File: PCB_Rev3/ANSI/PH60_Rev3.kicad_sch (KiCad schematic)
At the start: 46 parts, among them J1 USB_C_Receptacle_USB2.0_16P, J2 Conn_01x02, J3 Conn_01x02_Pin, J4 Conn_01x02_Pin, J6 Conn_01x02_Pin, SW1 SW_SPDT_321, U1 TLV62569DBV, U2 RP2040, U4 ETA6093, U6 W25Q16JVSS, Y1 Crystal_GND24

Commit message: Antenna update
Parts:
- added J8: Conn_01x02_Pin, Connector_PinHeader_2.00mm:PinHeader_1x02_P2.00mm_Vertical, symbol Connector:Conn_01x02_Pin
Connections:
- net RPI_TX: now reaches U2.40 (GPIO28_ADC2)
- net RPI_TX: now also J8.2 (Pin_2)
- net RPI_RX: now reaches U2.41 (GPIO29_ADC3)
- net RPI_RX: now also J8.1 (Pin_1)
- no-connect marks 12 -> 10
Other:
- moved on the sheet: J3, J4, J6

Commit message: vbus layout
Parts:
- added C27: 100uF, Capacitor_SMD:C_1206_3216Metric, symbol Device:C
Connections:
- net GND: now also C27.1
- net VBUS_SW: now also C27.2
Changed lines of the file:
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@@
 	)
 	(junction
+		(at 45.72 97.79)
+		(diameter 0)
+		(color 0 0 0 0)
+	)
+	(junction
 		(at 196.85 36.83)
 		(diameter 0)
@@
 	)
 	(symbol
+		(lib_id "power:GND")
+		(at 38.1 97.79 180)
+		(unit 1)
+		(exclude_from_sim no)
+		(in_bom yes)
+		(on_board yes)
+		(dnp no)
+		(fields_autoplaced yes)
+		(property "Reference" "#PWR041"
+			(at 38.1 91.44 0)
+			(effects
+				(font
+					(size 1.27 1.27)
+				)
+				(hide yes)
+			)
+		)
+		(property "Value" "GND"
+			(at 38.1 92.71 0)
+			(effects
+				(font
+					(size 1.27 1.27)
+				)
+			)
+		)
+		(property "Footprint" ""
+			(at 38.1 97.79 0)
+			(effects
+				(font
+					(size 1.27 1.27)
+				)
+				(hide yes)
+			)
+		)
+		(property "Datasheet" ""
+			(at 38.1 97.79 0)
+			(effects
+				(font
+					(size 1.27 1.27)
+				)
+				(hide yes)
+			)
+		)
+		(property "Description" "Power symbol creates a global label with name \"GND\" , ground"
+			(at 38.1 97.79 0)
+			(effects
+				(font
+					(size 1.27 1.27)
+				)
+				(hide yes)
+			)
+		)
+		(pin "1"
+		)
+		(instances
+			(project "PH60_Rev3"
+				(path "/dca0f898-8fdb-4522-a51d-f4f4238906e7"
+					(reference "#PWR041")
+					(unit 1)
+				)
+			)
+		)
+	)
+	(symbol
 		(lib_id "Device:C")
 		(at 113.03 43.18 0)
@@
 					(unit 1)
 				)
+			)
+		)
+	)
+	(symbol
+		(lib_id "Device:C")
+		(at 41.91 97.79 90)
+		(unit 1)
+		(exclude_from_sim no)
+		(in_bom no)
+		(on_board yes)
+		(dnp no)
+		(fields_autoplaced yes)
+		(property "Reference" "C27"
+			(at 41.91 90.17 90)
+			(effects
+				(font
+					(size 1.27 1.27)
+				)
+			)
+		)
+		(property "Value" "100uF"
+			(at 41.91 92.71 90)
+			(effects
+				(font
+					(size 1.27 1.27)
+				)
+			)
+		)
+		(property "Footprint" "Capacitor_SMD:C_1206_3216Metric"
+			(at 45.72 96.8248 0)
+			(effects
+				(font
+					(size 1.27 1.27)
+				)
+				(hide yes)
+			)
+		)
+		(property "Datasheet" "~"
+			(at 41.91 97.79 0)
+			(effects
+				(font
+					(size 1.27 1.27)
+				)
+				(hide yes)
+			)
+		)
+		(property "Description" "Unpolarized capacitor"
+			(at 41.91 97.79 0)
+			(effects
+				(font
+					(size 1.27 1.27)
+				)
+				(hide yes)
+			)
+		)
+		(pin "2"
+		)
+		(pin "1"
+		)
+		(instances
+			(project "PH60_Rev3"
+				(path "/dca0f898-8fdb-4522-a51d-f4f4238906e7"
+					(reference "C27")
+					(unit 1)
+				)

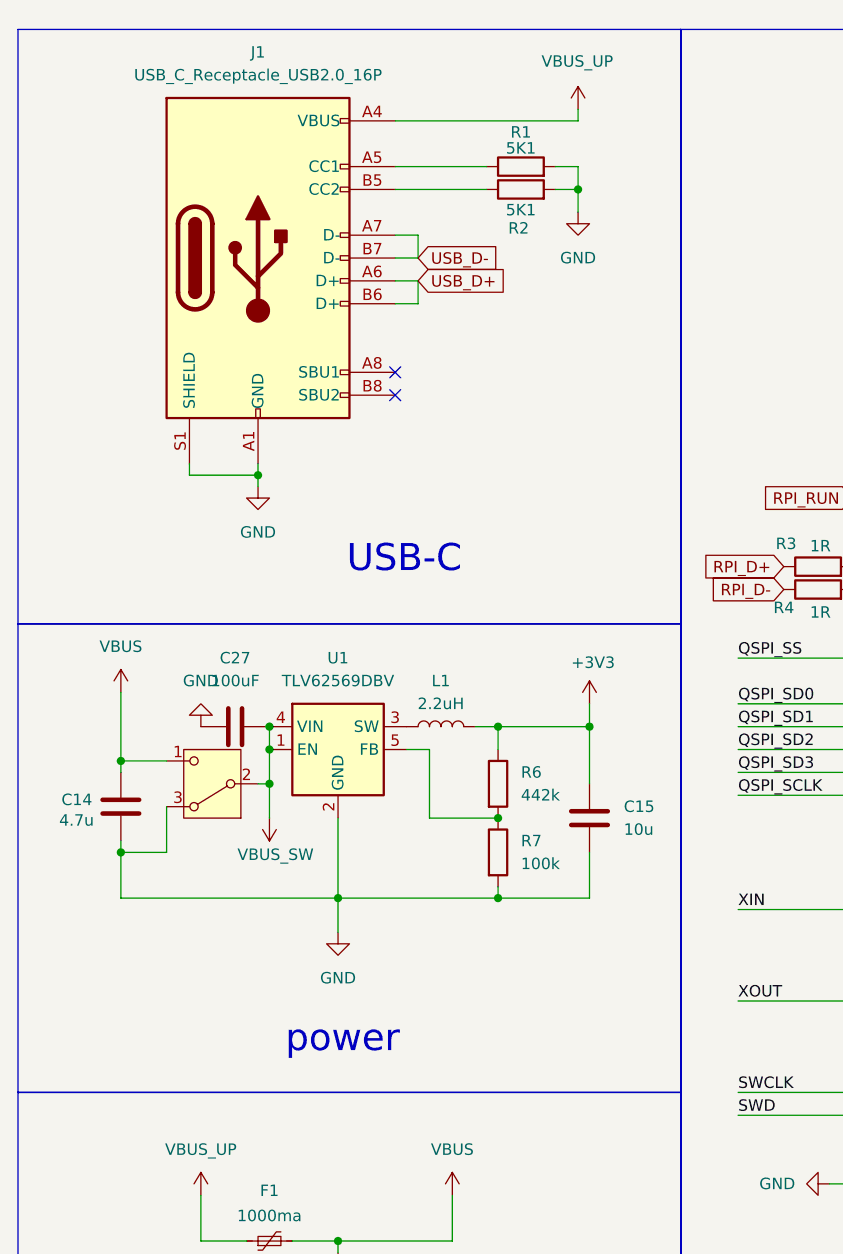
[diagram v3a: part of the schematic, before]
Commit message: drc三次
元件部分layout，移动一个电容，新增0f调试电容，电源轨修改
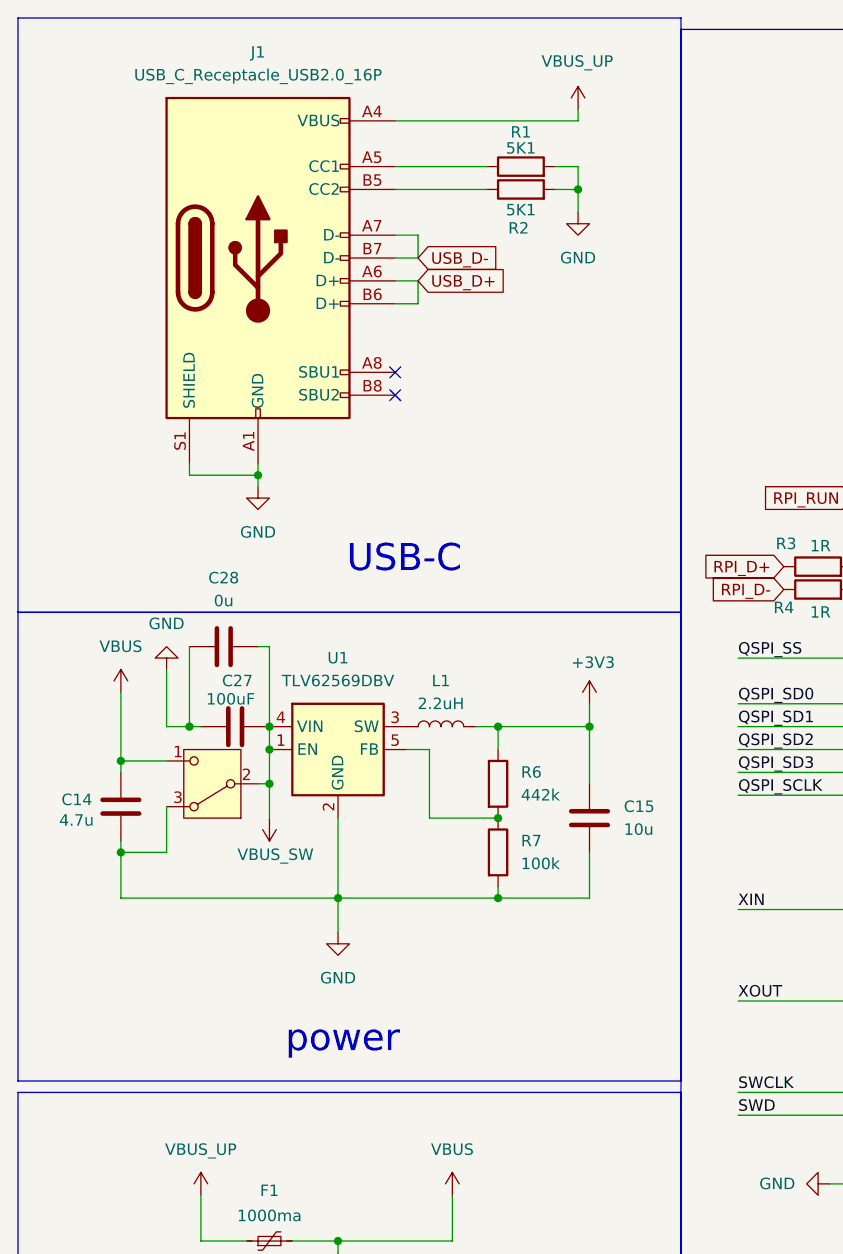
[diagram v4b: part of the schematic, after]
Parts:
- added C28: 0u, Capacitor_SMD:C_0402_1005Metric, symbol Device:C
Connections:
- net GND: now also C28.1
- net VBUS_SW: now also C28.2
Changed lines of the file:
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@@
 	)
 	(rectangle
-		(start 17.78 20.32)
-		(end 91.44 86.36)
+		(start 17.78 19.05)
+		(end 91.44 85.09)
 		(stroke
 			(width 0)
@@
 	)
 	(rectangle
-		(start 17.78 86.36)
-		(end 91.44 138.43)
+		(start 17.78 85.09)
+		(end 91.44 137.16)
 		(stroke
 			(width 0)
@@
 	)
 	(junction
+		(at 36.83 97.79)
+		(diameter 0)
+		(color 0 0 0 0)
+	)
+	(junction
 		(at 143.51 53.34)
 		(diameter 0)
@@
 	(wire
 		(pts
+			(xy 45.72 88.9) (xy 45.72 97.79)
+		)
+		(stroke
+			(width 0)
+			(type default)
+		)
+	)
+	(wire
+		(pts
 			(xy 80.01 29.21) (xy 80.01 30.48)
 		)
@@
 	(wire
 		(pts
+			(xy 45.72 88.9) (xy 44.45 88.9)
+		)
+		(stroke
+			(width 0)
+			(type default)
+		)
+	)
+	(wire
+		(pts
 			(xy 45.72 104.14) (xy 45.72 107.95)
 		)
@@
 	(wire
 		(pts
+			(xy 36.83 97.79) (xy 38.1 97.79)
+		)
+		(stroke
+			(width 0)
+			(type default)
+		)
+	)
+	(wire
+		(pts
 			(xy 55.88 227.33) (xy 63.5 227.33)
 		)
@@
 	(wire
 		(pts
+			(xy 34.29 91.44) (xy 34.29 97.79)
+		)
+		(stroke
+			(width 0)
+			(type default)
+		)
+	)
+	(wire
+		(pts
 			(xy 83.82 222.25) (xy 86.36 222.25)
 		)
@@
 	(wire
 		(pts
+			(xy 34.29 97.79) (xy 36.83 97.79)
+		)
+		(stroke
+			(width 0)
+			(type default)
+		)
+	)
+	(wire
+		(pts
+			(xy 36.83 88.9) (xy 36.83 97.79)
+		)
+		(stroke
+			(width 0)
+			(type default)
+		)
+	)
+	(wire
+		(pts
 			(xy 53.34 107.95) (xy 53.34 116.84)
 		)
@@
 	)
 	(symbol
+		(lib_id "Device:C")
+		(at 40.64 88.9 90)
+		(unit 1)
+		(exclude_from_sim no)
+		(in_bom yes)
+		(on_board yes)
+		(dnp no)
+		(fields_autoplaced yes)
+		(property "Reference" "C28"
+			(at 40.64 81.28 90)
+			(effects
+				(font
+					(size 1.27 1.27)
+				)
+			)
+		)
+		(property "Value" "0u"
+			(at 40.64 83.82 90)
+			(effects
+				(font
+					(size 1.27 1.27)
+				)
+			)
+		)
+		(property "Footprint" "Capacitor_SMD:C_0402_1005Metric"
+			(at 44.45 87.9348 0)
+			(effects
+				(font
+					(size 1.27 1.27)
+				)
+				(hide yes)
+			)
+		)
+		(property "Datasheet" "~"
+			(at 40.64 88.9 0)
+			(effects
+				(font
+					(size 1.27 1.27)
+				)
+				(hide yes)
+			)
+		)
+		(property "Description" "Unpolarized capacitor"
+			(at 40.64 88.9 0)
+			(effects
+				(font
+					(size 1.27 1.27)
+				)
+				(hide yes)
+			)
+		)
+		(pin "2"
+		)
+		(pin "1"
+		)
+		(instances
+			(project "PH60_Rev3"
+				(path "/dca0f898-8fdb-4522-a51d-f4f4238906e7"
+					(reference "C28")
+					(unit 1)
+				)
+			)
+		)
+	)
+	(symbol
 		(lib_id "Device:R")
 		(at 198.12 132.08 90)
@@
 	(symbol
 		(lib_id "power:GND")
-		(at 38.1 97.79 180)
+		(at 34.29 91.44 0)
+		(mirror x)
 		(unit 1)
 		(exclude_from_sim no)
@@
 		(on_board yes)
 		(dnp no)
-		(fields_autoplaced yes)
 		(property "Reference" "#PWR041"
-			(at 38.1 91.44 0)
+			(at 34.29 85.09 0)
 			(effects
 				(font
@@
 		)
 		(property "Value" "GND"
-			(at 38.1 92.71 0)
+			(at 34.29 86.36 0)
 			(effects
 				(font
@@
 		)
 		(property "Footprint" ""
-			(at 38.1 97.79 0)
+			(at 34.29 91.44 0)
 			(effects
 				(font
@@
 		)
 		(property "Datasheet" ""
-			(at 38.1 97.79 0)
+			(at 34.29 91.44 0)
 			(effects
 				(font
@@
 		)
 		(property "Description" "Power symbol creates a global label with name \"GND\" , ground"
-			(at 38.1 97.79 0)
+			(at 34.29 91.44 0)
 			(effects
 				(font
@@
 		(on_board yes)
 		(dnp no)
-		(fields_autoplaced yes)
 		(property "Reference" "C27"
-			(at 41.91 90.17 90)
+			(at 42.164 92.71 90)
 			(effects
 				(font
@@
 		)
 		(property "Value" "100uF"
-			(at 41.91 92.71 90)
+			(at 41.402 94.742 90)
 			(effects
 				(font

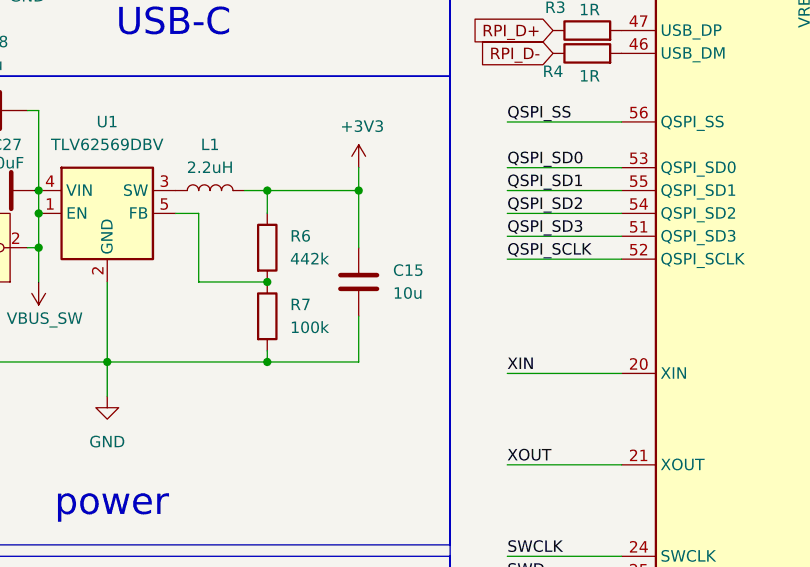
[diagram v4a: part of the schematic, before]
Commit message: 四次drc
gnd过孔精简，3v3添加0F调试电容
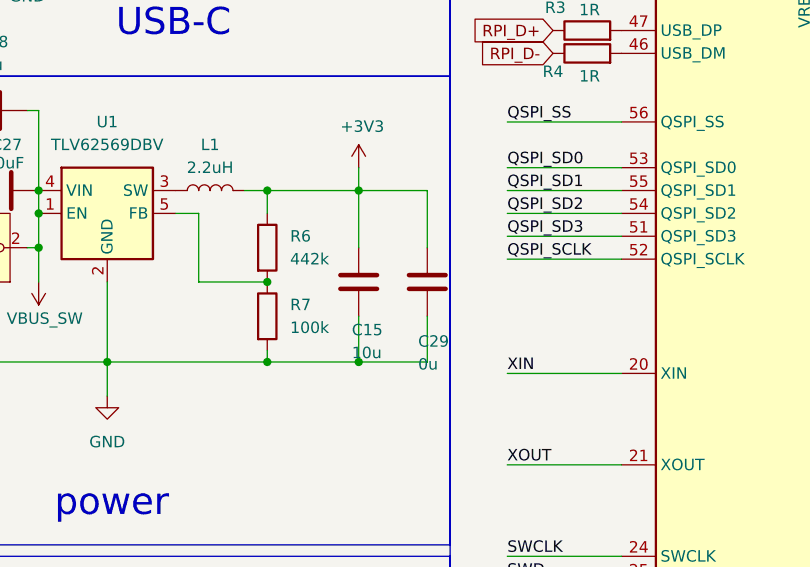
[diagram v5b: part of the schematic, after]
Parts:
- added C29: 0u, Capacitor_SMD:C_0402_1005Metric, symbol Device:C
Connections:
- net +3V3: now also C29.1
- net GND: now also C29.2
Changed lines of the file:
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@@
 	)
 	(junction
+		(at 81.28 116.84)
+		(diameter 0)
+		(color 0 0 0 0)
+	)
+	(junction
 		(at 71.12 107.95)
 		(diameter 0)
@@
 	(wire
 		(pts
+			(xy 81.28 97.79) (xy 88.9 97.79)
+		)
+		(stroke
+			(width 0)
+			(type default)
+		)
+	)
+	(wire
+		(pts
 			(xy 226.06 124.46) (xy 226.06 127)
 		)
@@
 	(wire
 		(pts
+			(xy 88.9 104.14) (xy 88.9 97.79)
+		)
+		(stroke
+			(width 0)
+			(type default)
+		)
+	)
+	(wire
+		(pts
 			(xy 45.72 88.9) (xy 45.72 97.79)
 		)
@@
 	(wire
 		(pts
+			(xy 81.28 116.84) (xy 88.9 116.84)
+		)
+		(stroke
+			(width 0)
+			(type default)
+		)
+	)
+	(wire
+		(pts
 			(xy 121.92 53.34) (xy 130.81 53.34)
 		)
@@
 	(wire
 		(pts
+			(xy 88.9 111.76) (xy 88.9 116.84)
+		)
+		(stroke
+			(width 0)
+			(type default)
+		)
+	)
+	(wire
+		(pts
 			(xy 53.34 154.94) (xy 66.04 154.94)
 		)
@@
 	)
 	(symbol
+		(lib_id "Device:C")
+		(at 88.9 107.95 0)
+		(unit 1)
+		(exclude_from_sim no)
+		(in_bom yes)
+		(on_board yes)
+		(dnp no)
+		(property "Reference" "C29"
+			(at 87.884 114.554 0)
+			(effects
+				(font
+					(size 1.27 1.27)
+				)
+				(justify left)
+			)
+		)
+		(property "Value" "0u"
+			(at 87.884 117.094 0)
+			(effects
+				(font
+					(size 1.27 1.27)
+				)
+				(justify left)
+			)
+		)
+		(property "Footprint" "Capacitor_SMD:C_0402_1005Metric"
+			(at 89.8652 111.76 0)
+			(effects
+				(font
+					(size 1.27 1.27)
+				)
+				(hide yes)
+			)
+		)
+		(property "Datasheet" "~"
+			(at 88.9 107.95 0)
+			(effects
+				(font
+					(size 1.27 1.27)
+				)
+				(hide yes)
+			)
+		)
+		(property "Description" "Unpolarized capacitor"
+			(at 88.9 107.95 0)
+			(effects
+				(font
+					(size 1.27 1.27)
+				)
+				(hide yes)
+			)
+		)
+		(pin "2"
+		)
+		(pin "1"
+		)
+		(instances
+			(project "PH60_Rev3"
+				(path "/dca0f898-8fdb-4522-a51d-f4f4238906e7"
+					(reference "C29")
+					(unit 1)
+				)
+			)
+		)
+	)
+	(symbol
 		(lib_id "power:GND")
 		(at 107.95 148.59 270)
@@
 		(on_board yes)
 		(dnp no)
-		(fields_autoplaced yes)
 		(property "Reference" "C15"
-			(at 85.09 106.6799 0)
+			(at 80.518 113.284 0)
 			(effects
 				(font
@@
 		)
 		(property "Value" "10u"
-			(at 85.09 109.2199 0)
+			(at 80.518 115.824 0)
 			(effects
 				(font

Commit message: Routing update
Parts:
- J4: footprint Connector_PinHeader_2.00mm:PinHeader_1x02_P2.00mm_Vertical -> Connector_PinHeader_1.27mm:PinHeader_1x02_P1.27mm_Vertical
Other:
- moved on the sheet: C14, C15, C27, C28, C29, L1, R6, R7, U1

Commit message: drc确认
1
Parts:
- C28, C29: now left out of the parts list
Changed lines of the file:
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@@
 		(unit 1)
 		(exclude_from_sim no)
-		(in_bom yes)
+		(in_bom no)
 		(on_board yes)
 		(dnp no)
@@
 		(unit 1)
 		(exclude_from_sim no)
-		(in_bom yes)
+		(in_bom no)
 		(on_board yes)
 		(dnp no)

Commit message: 3v3电源修改
1
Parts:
- C28: value 0u -> 10u; now in the parts list
- C29: value 0u -> 100u; now in the parts list
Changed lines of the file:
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@@
 		(unit 1)
 		(exclude_from_sim no)
-		(in_bom no)
+		(in_bom yes)
 		(on_board yes)
 		(dnp no)
@@
 			)
 		)
-		(property "Value" "0u"
+		(property "Value" "100u"
 			(at 85.09 112.522 0)
 			(effects
@@
 		(unit 1)
 		(exclude_from_sim no)
-		(in_bom no)
+		(in_bom yes)
 		(on_board yes)
 		(dnp no)
@@
 			)
 		)
-		(property "Value" "0u"
+		(property "Value" "10u"
 			(at 38.1 90.17 90)
 			(effects
